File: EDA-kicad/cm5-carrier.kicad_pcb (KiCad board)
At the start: 2 copper layers, 80 x 150 mm, 85 parts, among them J1 SJ2-35894B-SMT-TR, J2 USBC-3-2-fix-USB4056-03-A_REV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, J3 SIM-G85D1160022HHR, J4 FINGER, SW1 CHP-041B, SW2 PROG, SW3 VOL-, SW4 VOL+, SW5 POW, U2 BAT-CONNECTOR-FLTS22WR00, U3 BAT-MONITOR-BQ27530YZFT-G1, U4 CHARGER-SWITCHER-BQ25303JRTER, U5 Flash-LED-Lumiled, U6 FPC15pin-1mm-pitch-F52Q-1A7H1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, U7 CODEC-TLV320AIC3204IRHBR, U8 DAC-TLV320DAC3100IRHBR, U9 GSM-GPS-EC25VFA-512-STD

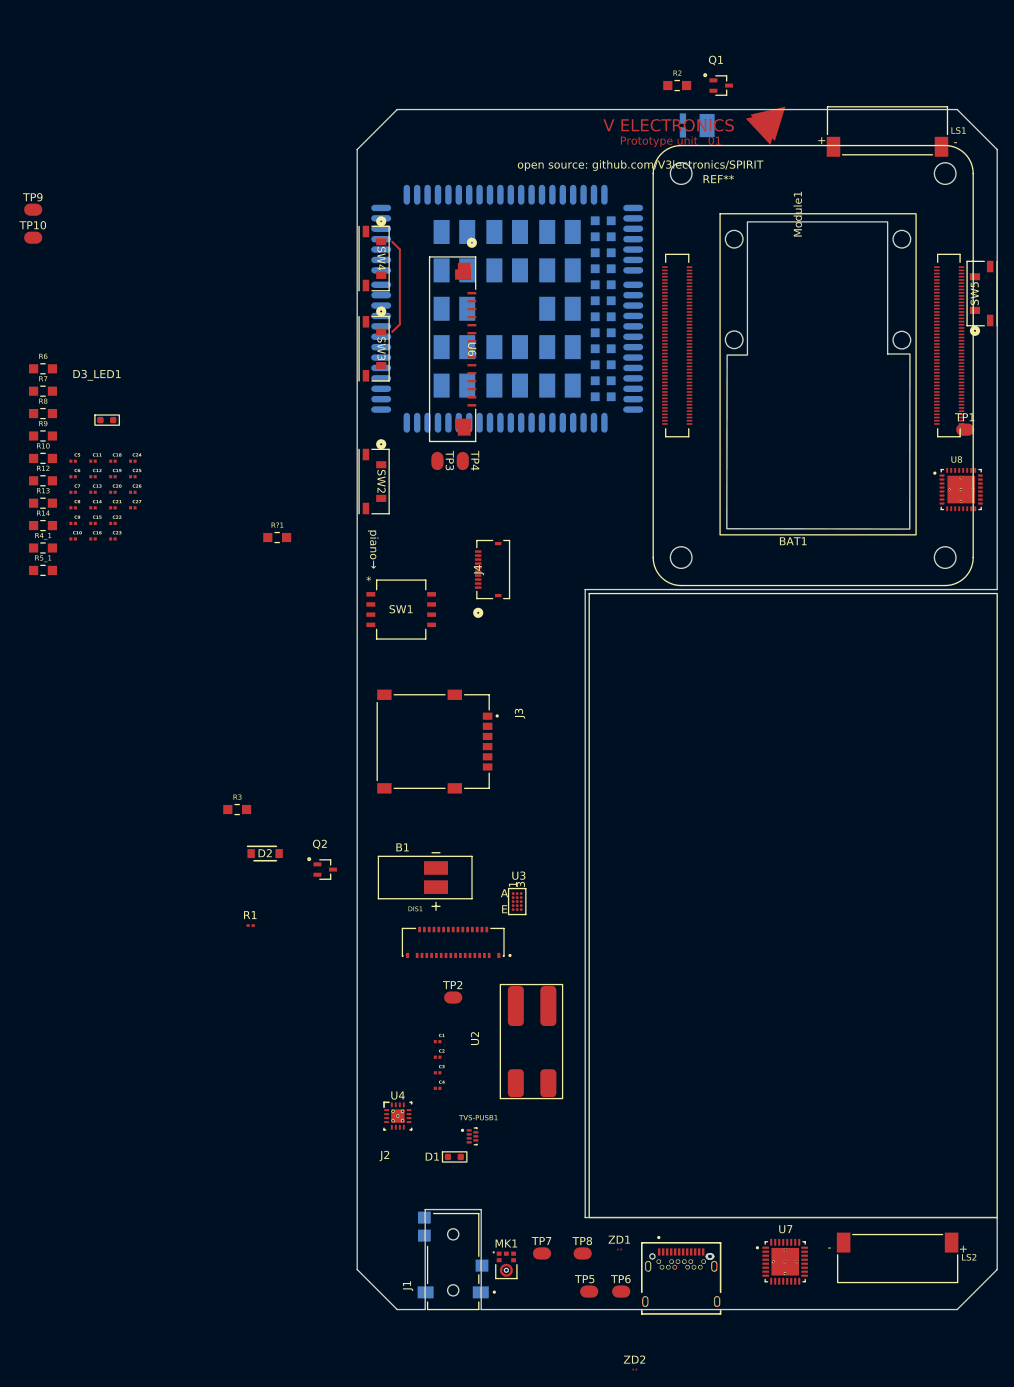
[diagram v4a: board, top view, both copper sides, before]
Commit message: fully sync pcb to schematic, fix some models
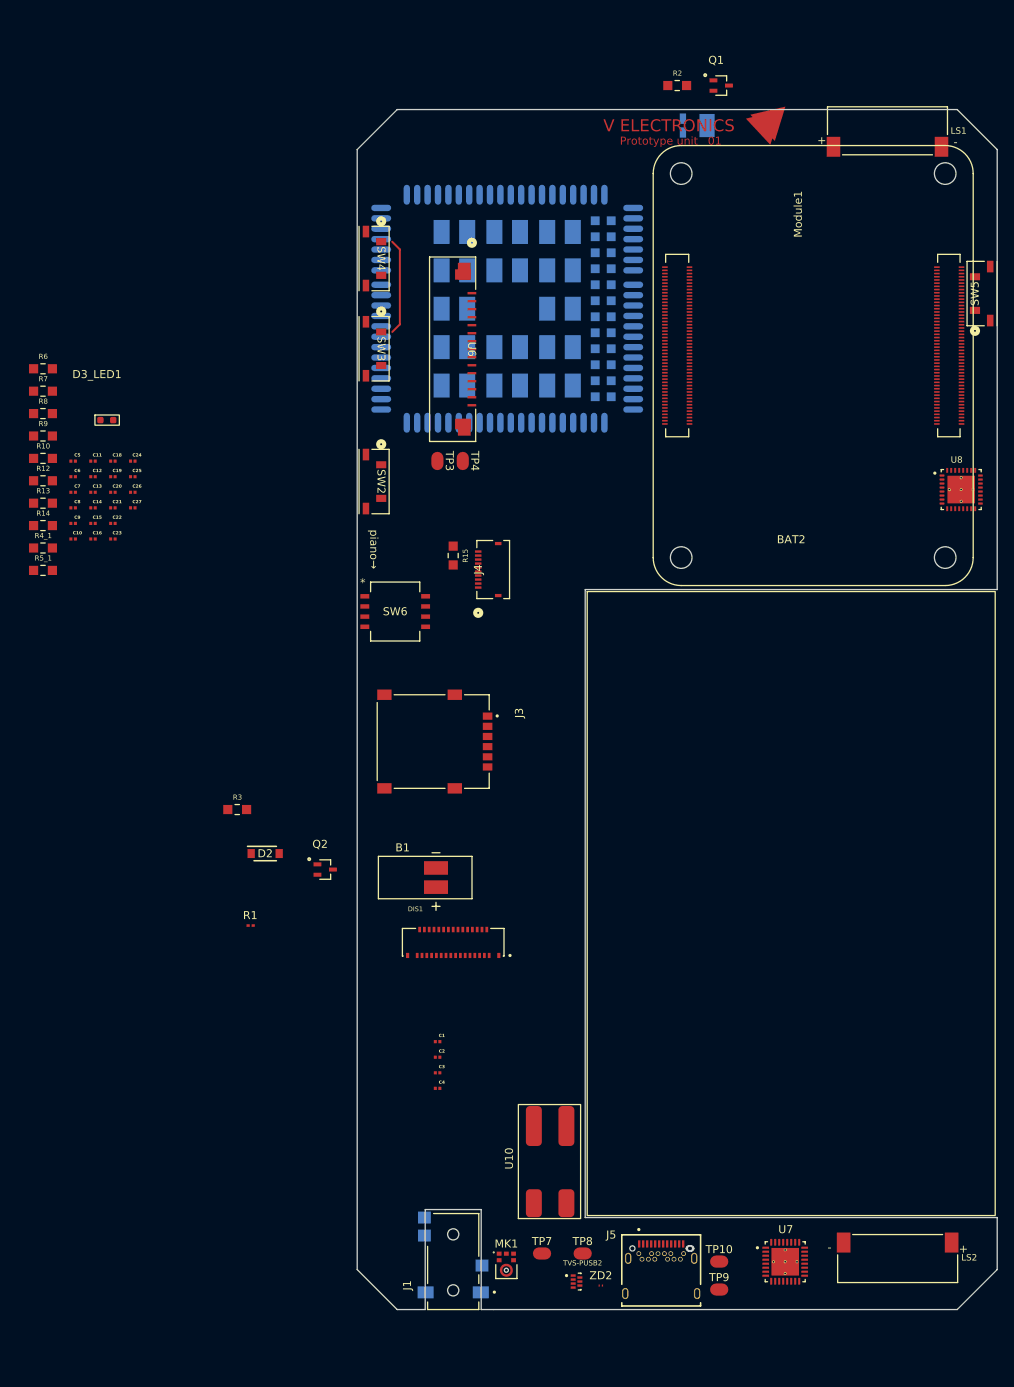
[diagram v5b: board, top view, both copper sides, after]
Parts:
- removed BAT1: battery_LP685077JU, SPIRIT-footprints:battery_37V3500mAhLP685077JU
- removed D1: LED-INDICATOR, SPIRIT-footprints:LED-INDICATOR
- removed J2: USBC-3-2-fix-USB4056-03-A_REVA2, SPIRIT-footprints:USBC-3-2-fix-GCT_USB4056-03-A_REVA2
- removed R?1: 1K-05W-0805-RES_ERJP06J102V, SPIRIT-footprints:1K-05W-0805-RES_ERJP06J102V
- removed REF**: 64MP-Arducam, SPIRIT-footprints:64MP-Arducam
- removed SW1: CHP-041B, SPIRIT-footprints:pianoCHP-041B_NDC
- removed TP1, TP2, TP5, TP6: test-pad-1, SPIRIT-footprints:test-pad-1
- removed TVS-PUSB1: ~, SPIRIT-footprints:TVS-array-IC_PUSB3AB6Z
- removed U2: BAT-CONNECTOR-FLTS22WR00, SPIRIT-footprints:BAT-CONNECTOR-FLTS22WR00
- removed U3: BAT-MONITOR-BQ27530YZFT-G1, SPIRIT-footprints:BAT-MONITOR-YZF15_TEX
- removed U4: CHARGER-SWITCHER-BQ25303JRTER, SPIRIT-footprints:CHARGER-SWITCHER-RTE0016C
- removed ZD1: protection-PESD5V0C1USFYL, SPIRIT-footprints:USB-ESD-protection-diode-PESD5V0C1USFYL-SOD962-2_DSN0603-2_NEX
- added BAT2: battery_37V3500mAhLP685077JU, SPIRIT-footprints:battery_37V3500mAhLP685077JU, F.Cu at (109.2, 96.2)
- added J5: USBC-3-2-fix-USB4056-03-A_REVA2, SPIRIT-footprints:USBC-3-2-fix-GCT_USB4056-03-A_REVA2, F.Cu at (93.0, 179.0)
- added R15: 270K-05W-0805-RES_ERJP06J102V, SPIRIT-footprints:1K-05W-0805-RES_ERJP06J102V, F.Cu at (67.0, 86.8)
- added SW6: CHP-041B, SPIRIT-footprints:pianoCHP-041B_NDC, F.Cu at (59.8, 93.8)
- added TVS-PUSB2: ~, SPIRIT-footprints:TVS-array-IC_PUSB3AB6Z, F.Cu at (82.4, 177.5)
- added U10: BAT-CONNECTOR-FLTS22WR00, SPIRIT-footprints:BAT-CONNECTOR-FLTS22WR00, F.Cu at (72.5, 162.1)
- moved TP9 159.9 mm to (100.2, 177.5)
- moved TP10 154.1 mm to (100.2, 174.0)
- moved G*** 18.1 mm to (67.0, 33.2)
- moved ZD2 11.3 mm to (85.5, 178.0)
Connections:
- J4 pad 6: unconnected-(J4-Pad6) -> SPI0_RDY
- J4 pad 7: unconnected-(J4-Pad7) -> VCC
- R2 pad 1: Net-(Module1A-GPIO22) -> GPIO22
- R3 pad 1: Net-(Module1A-GPIO27) -> GPIO27
- SW2 pad 2: Net-(Module1A-GPIO17) -> GPIO17
- SW3 pad 2: Net-(Module1A-GPIO4) -> GPIO4
- SW4 pad 2: Net-(Module1A-GPIO3) -> GPIO3
- SW5 pad 2: Net-(Module1A-GPIO2) -> GPIO2
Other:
- board text removed: "open source: github.com/V3lectronics/SPIRIT"
